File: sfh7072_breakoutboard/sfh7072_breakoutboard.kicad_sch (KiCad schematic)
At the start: 10 parts, among them J1 Conn_01x04_Pin, J2 Conn_01x05_Pin

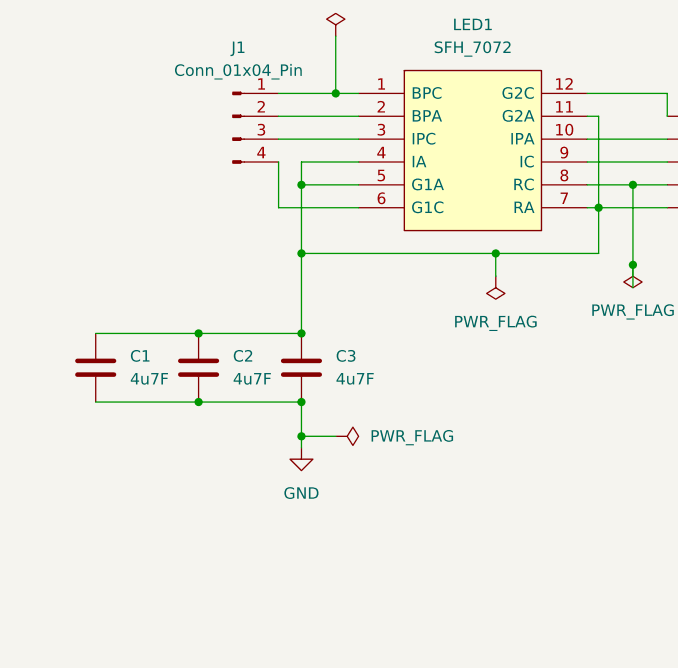
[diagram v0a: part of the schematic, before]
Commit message: sfh7072 cap location updates
Signed-off-by: Mika Laitio <lamikr@gmail.com>
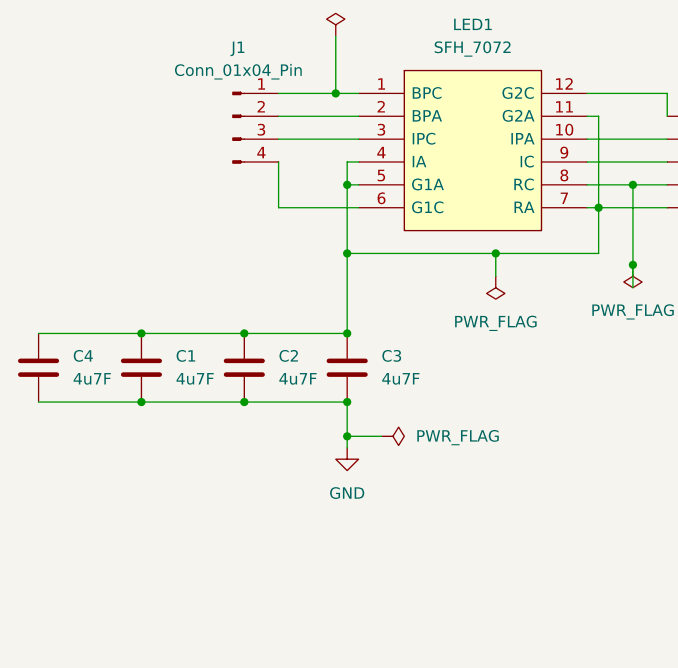
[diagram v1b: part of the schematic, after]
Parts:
- added C4: 4u7F, Capacitor_SMD:C_0603_1608Metric, symbol Device:C
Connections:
- net GND: now also C4.2
- net at C1.1, C2.1, C3.1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: now also C4.1
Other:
- moved on the sheet: C1, C2, C3

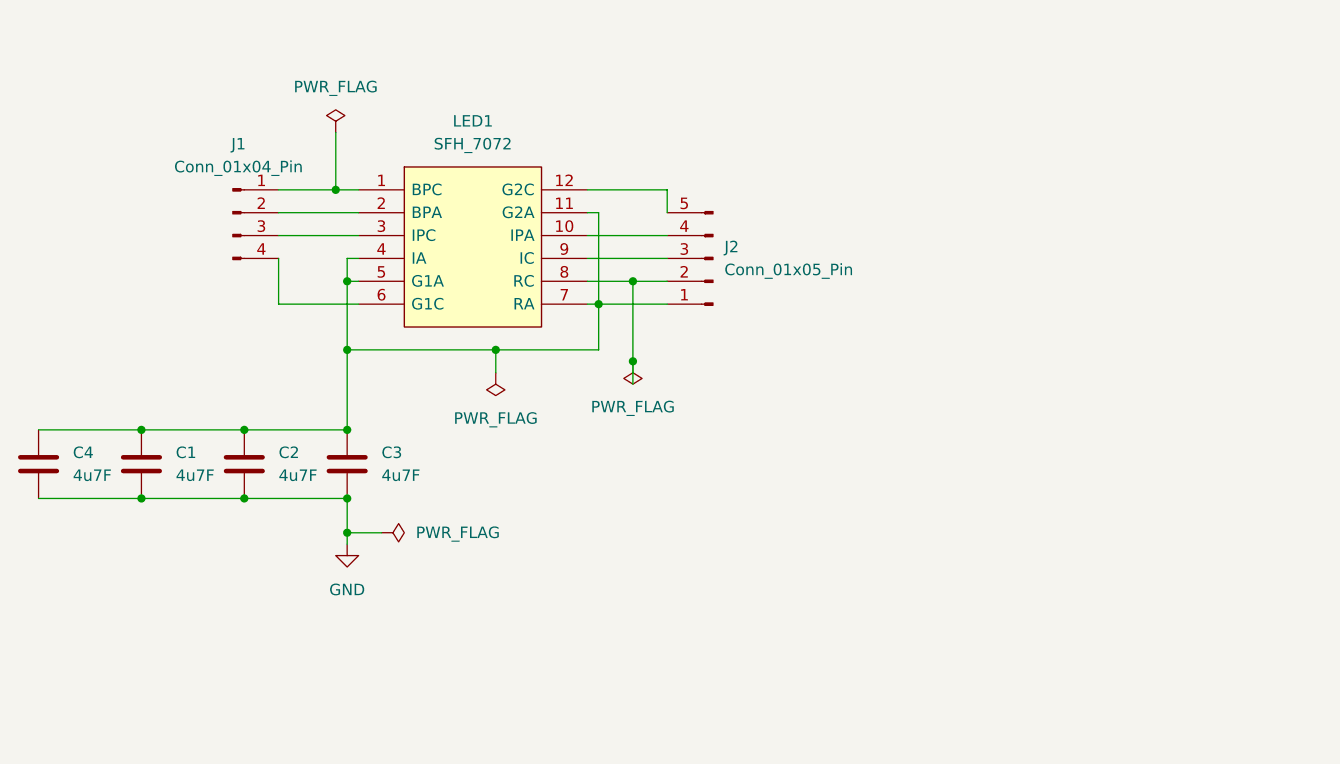
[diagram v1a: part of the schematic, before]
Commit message: sfh7072 breakoutboard and pcb manufacturing
Signed-off-by: Mika Laitio <lamikr@gmail.com>
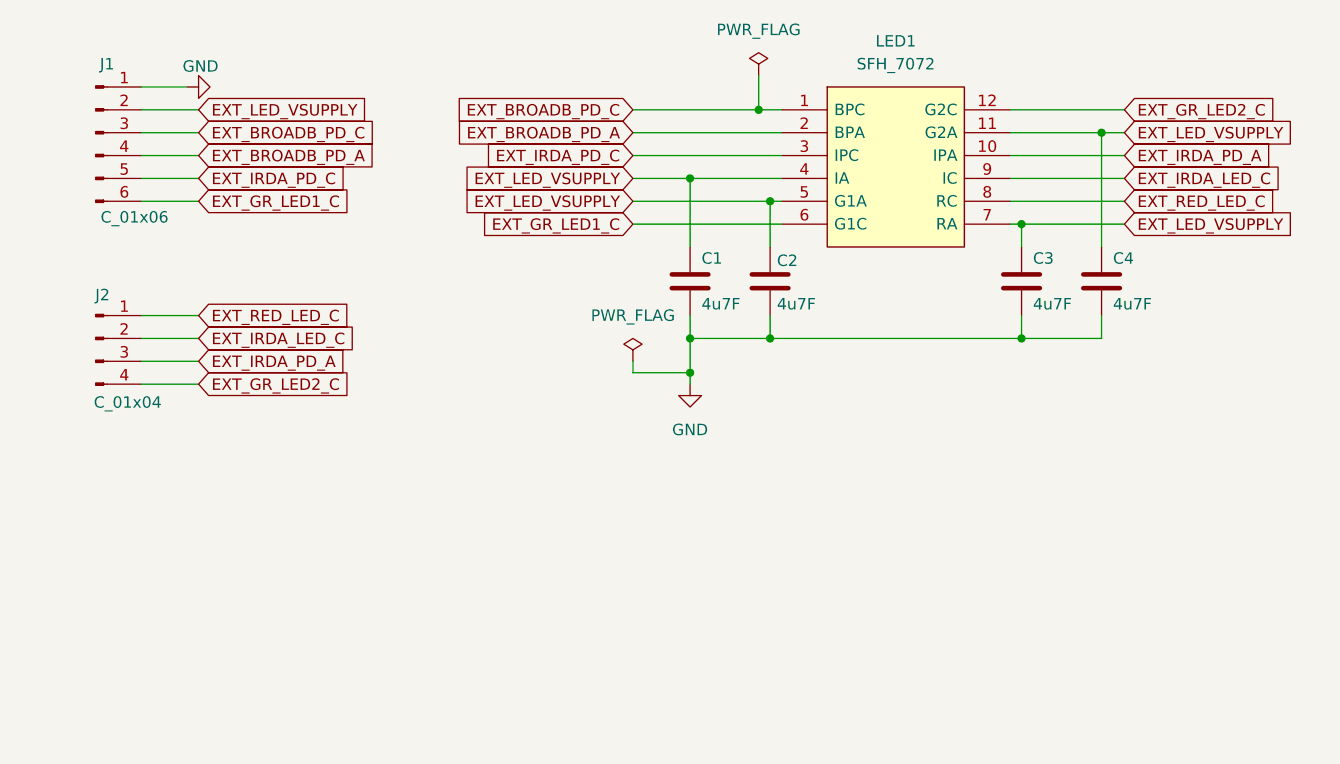
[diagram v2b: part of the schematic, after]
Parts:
- removed J1: Conn_01x04_Pin, Connector_PinHeader_2.54mm:PinHeader_1x04_P2.54mm_Vertical, symbol Connector:Conn_01x04_Pin
- removed J2: Conn_01x05_Pin, Connector_PinHeader_2.54mm:PinHeader_1x05_P2.54mm_Vertical, symbol Connector:Conn_01x05_Pin
- added J1: C_01x06, Connector_PinHeader_2.54mm:PinHeader_1x06_P2.54mm_Vertical, symbol Connector:Conn_01x06_Pin
- added J2: C_01x04, Connector_PinHeader_2.54mm:PinHeader_1x04_P2.54mm_Vertical, symbol Connector:Conn_01x04_Pin
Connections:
- net GND: now also J1.1 (Pin_1)
- net EXT_LED_VSUPPLY: now reaches C1.1, C2.1, C3.1, C4.1, LED1.11 (G2A), LED1.4 (IA), LED1.5 (G1A), LED1.7 (RA)
- net EXT_LED_VSUPPLY: now also J1.2 (Pin_2)
- net EXT_RED_LED_C: now reaches LED1.8 (RC)
- net EXT_RED_LED_C: now also J2.1 (Pin_1)
- net EXT_IRDA_LED_C: now reaches LED1.9 (IC)
- net EXT_IRDA_LED_C: now also J2.2 (Pin_2)
- net EXT_IRDA_PD_A: now reaches LED1.10 (IPA)
- net EXT_IRDA_PD_A: now also J2.3 (Pin_3)
- net EXT_GR_LED2_C: now reaches LED1.12 (G2C)
- net EXT_GR_LED2_C: now also J2.4 (Pin_4)
- net EXT_BROADB_PD_C: now reaches LED1.1 (BPC)
- net EXT_BROADB_PD_C: now also J1.3 (Pin_3)
- net EXT_BROADB_PD_A: now reaches LED1.2 (BPA)
- net EXT_BROADB_PD_A: now also J1.4 (Pin_4)
- net EXT_IRDA_PD_C: now reaches LED1.3 (IPC)
- net EXT_IRDA_PD_C: now also J1.5 (Pin_5)
- net EXT_GR_LED1_C: now reaches LED1.6 (G1C)
- net EXT_GR_LED1_C: now also J1.6 (Pin_6)
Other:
- moved on the sheet: C1, C2, C3, C4, LED1

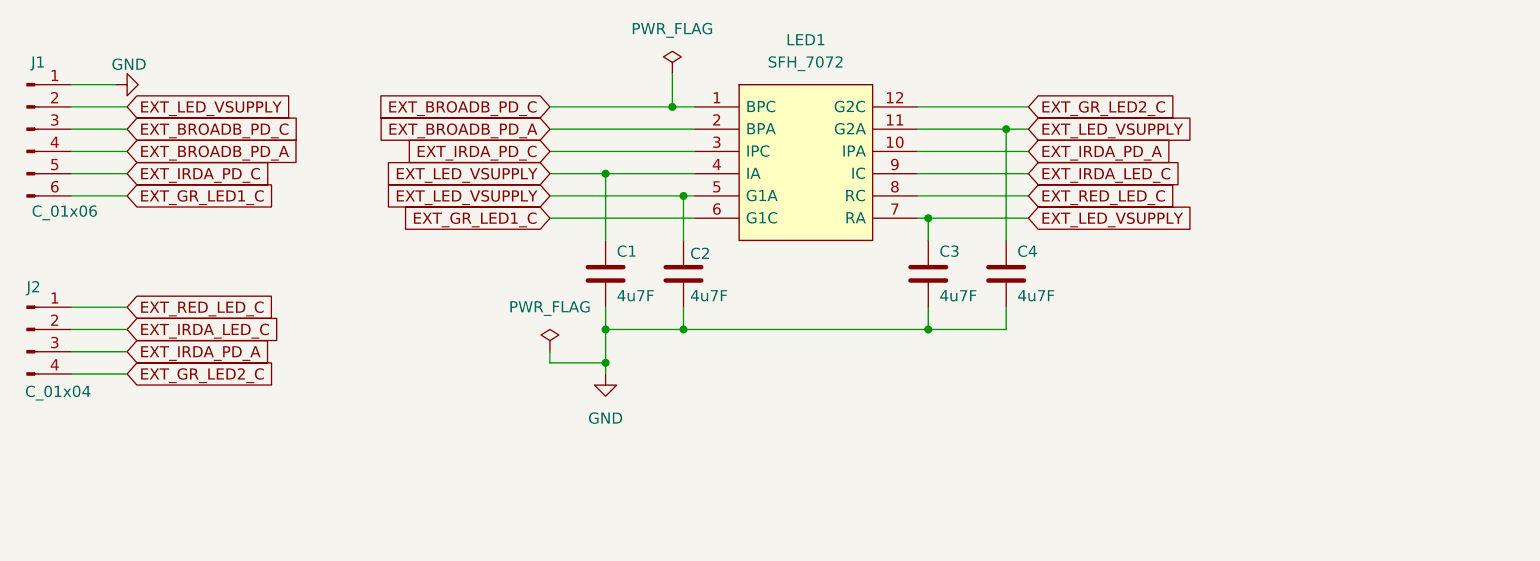
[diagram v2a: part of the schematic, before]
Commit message: sfh7072 board with separate anode for all leds
- separate anode and cathode connector for all leds
  and photodiodes

Signed-off-by: Mika Laitio <lamikr@gmail.com>
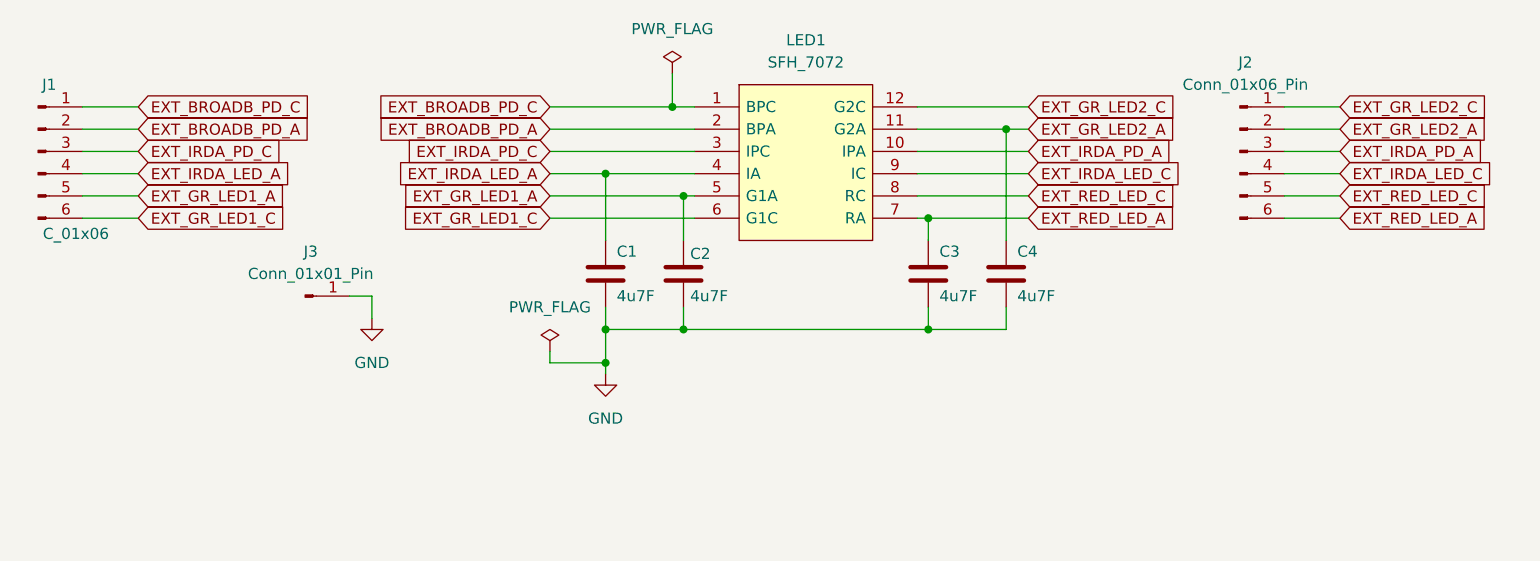
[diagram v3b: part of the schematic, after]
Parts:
- removed J2: C_01x04, Connector_PinHeader_2.54mm:PinHeader_1x04_P2.54mm_Vertical, symbol Connector:Conn_01x04_Pin
- added J2: Conn_01x06_Pin, Connector_PinHeader_2.54mm:PinHeader_1x06_P2.54mm_Vertical, symbol Connector:Conn_01x06_Pin
- added J3: Conn_01x01_Pin, Connector_PinHeader_1.27mm:PinHeader_1x01_P1.27mm_Vertical, symbol Connector:Conn_01x01_Pin
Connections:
- net EXT_BROADB_PD_A: now also J1.2 (Pin_2); no longer J1.4 (Pin_4)
- net EXT_BROADB_PD_C: now also J1.1 (Pin_1); no longer J1.3 (Pin_3)
- net EXT_GR_LED2_C: now also J2.1 (Pin_1)
- net EXT_IRDA_LED_C: now also J2.4 (Pin_4)
- net EXT_IRDA_PD_A: now also J2.3 (Pin_3)
- net EXT_IRDA_PD_C: now also J1.3 (Pin_3); no longer J1.5 (Pin_5)
- net EXT_RED_LED_C: now also J2.5 (Pin_5)
- net GND: now also J3.1 (Pin_1); no longer J1.1 (Pin_1)
- removed net EXT_LED_VSUPPLY: C1.1, C2.1, C3.1, C4.1, J1.2 (Pin_2), LED1.11 (G2A), LED1.4 (IA), LED1.5 (G1A), LED1.7 (RA)
- new net EXT_GR_LED1_A: C2.1, J1.5 (Pin_5), LED1.5 (G1A)
- new net EXT_GR_LED2_A: C4.1, J2.2 (Pin_2), LED1.11 (G2A)
- new net EXT_IRDA_LED_A: C1.1, J1.4 (Pin_4), LED1.4 (IA)
- new net EXT_RED_LED_A: C3.1, J2.6 (Pin_6), LED1.7 (RA)
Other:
- moved on the sheet: J1
